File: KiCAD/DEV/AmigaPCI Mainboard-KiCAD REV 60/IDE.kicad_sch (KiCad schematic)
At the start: 55 parts, among them CN900 PRIMARY IDE, CN901 SECONDARY IDE, Q900 MMBT3906, U220 74LVC08, U815 74LVC08, U900 74LVC245, U901 74LVC245, U902 74LVC245, U903 74LVC245, U904 74LVC245, U905 74LVC245, U906 74LVC373, U907 74LVC373

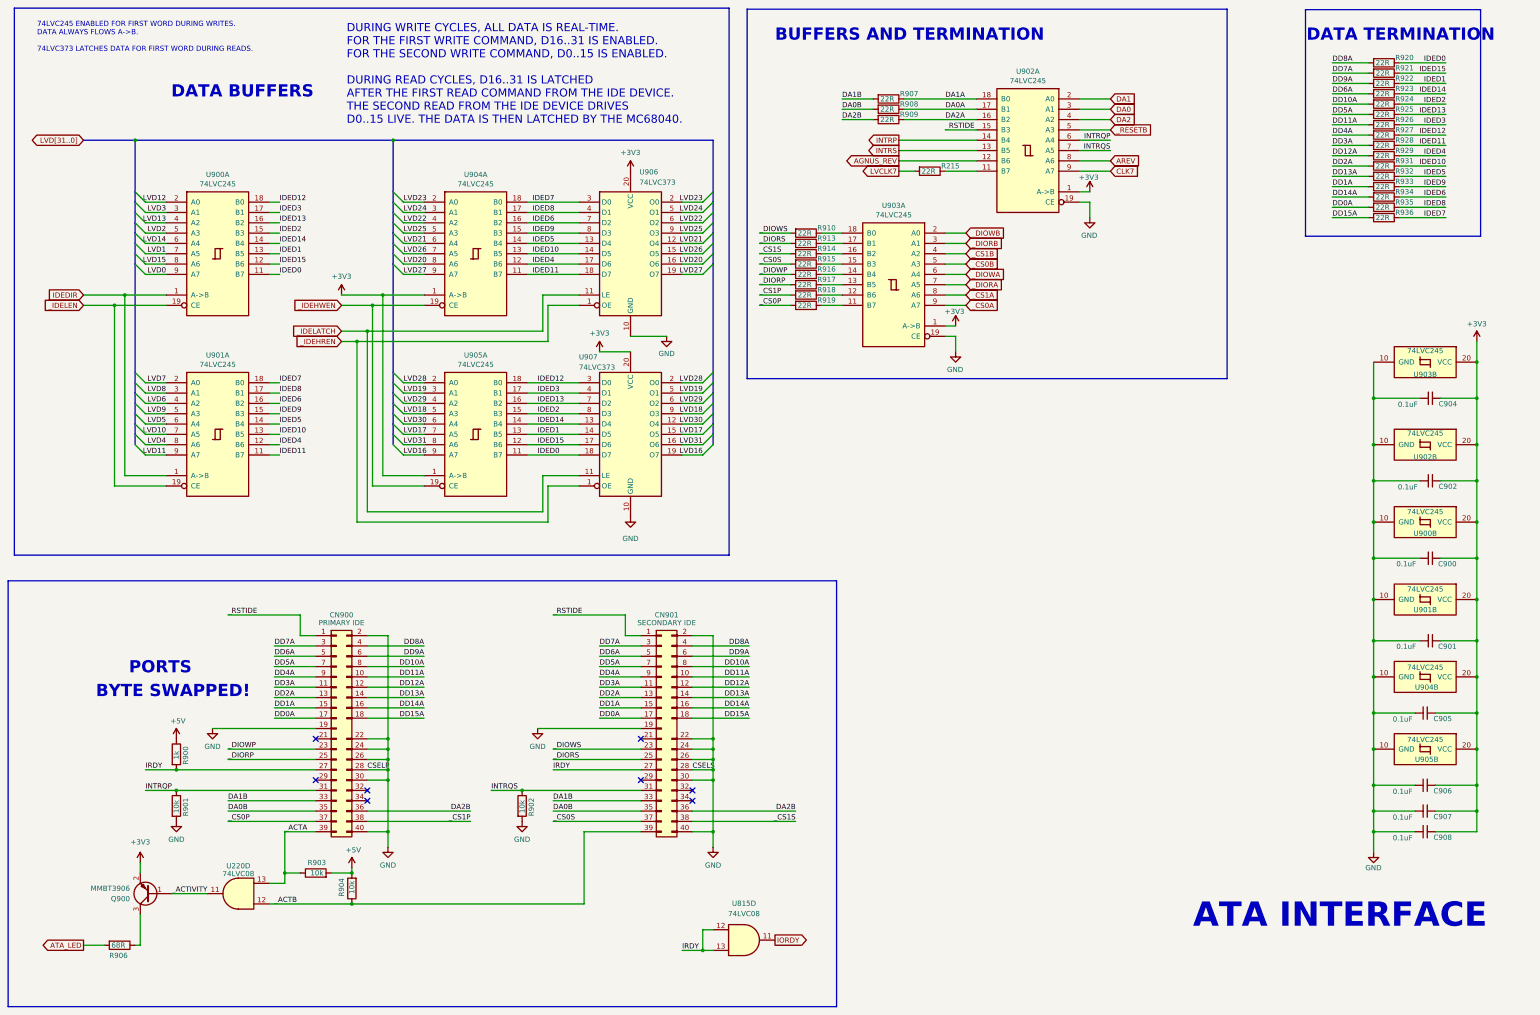
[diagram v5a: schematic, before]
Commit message: APCI Rev 6.0 Work
Added flash and i2c, USB now powered by standbay rail.
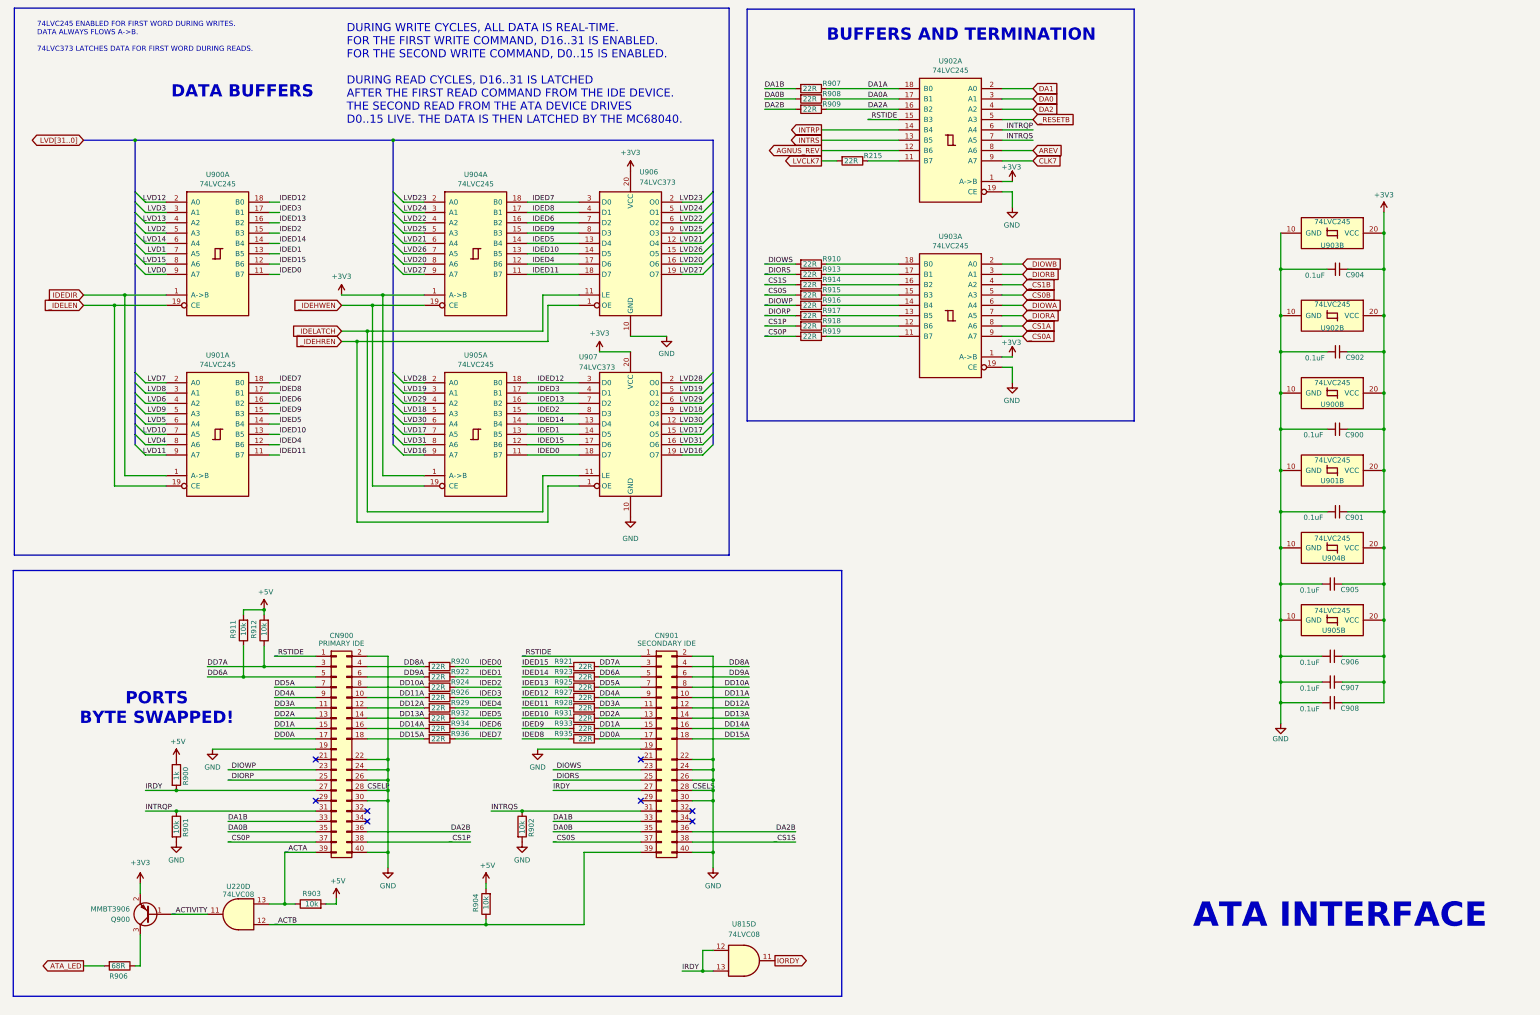
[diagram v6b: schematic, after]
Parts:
- added R911, R912: 10k, Resistor_SMD:R_0603_1608Metric, symbol Device:R
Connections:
- net +5V: now also R911.2, R912.2
- net DD6A: now also R911.1
- net DD7A: now also R912.1
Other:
- note added: "DURING WRITE CYCLES, ALL DATA IS REAL-TIME. FOR THE FIRST WRITE COMMAND, D16..31 IS ENABLED. FOR THE SECOND WRITE COMMAND, D0..15 IS ENABLED. DURING READ CYCLES, D16..31 IS LATCHED AFTER THE FIRST READ COMMAND FROM THE IDE DEVICE. THE SECOND READ FROM THE ATA DEVICE DRIVES D0..15 LIVE. THE DATA IS THEN LATCHED BY THE MC68040."
- note added: "PORTS BYTE SWAPPED!"
- note removed: "BYTE SWAPPED!"
- note removed: "DATA TERMINATION"
- note removed: "DURING WRITE CYCLES, ALL DATA IS REAL-TIME. FOR THE FIRST WRITE COMMAND, D16..31 IS ENABLED. FOR THE SECOND WRITE COMMAND, D0..15 IS ENABLED. DURING READ CYCLES, D16..31 IS LATCHED AFTER THE FIRST READ COMMAND FROM THE IDE DEVICE. THE SECOND READ FROM THE IDE DEVICE DRIVES D0..15 LIVE. THE DATA IS THEN LATCHED BY THE MC68040."
- note removed: "PORTS"
- moved on the sheet: C900, C901, C902, C904, C905, C906, C907, C908, CN900, CN901, Q900, R215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

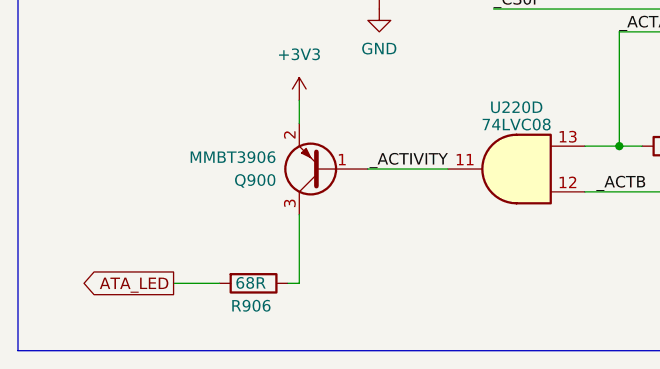
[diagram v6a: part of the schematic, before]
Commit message: APCI Added _LBEN pullup.
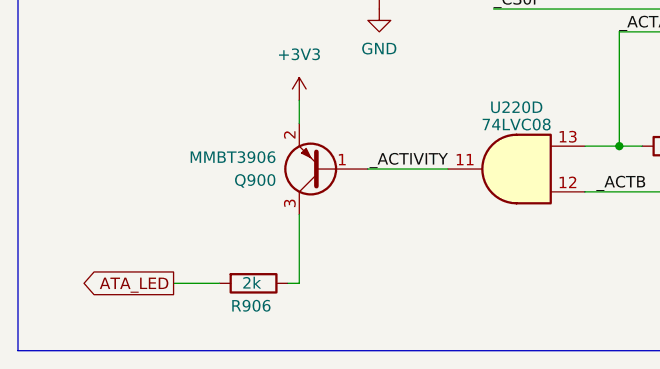
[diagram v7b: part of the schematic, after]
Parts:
- R906: value 68R -> 2k
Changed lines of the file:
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@@
 			)
 		)
-		(property "Value" "68R"
-			(at 46.228 255.27 90)
+		(property "Value" "2k"
+			(at 46.99 255.27 90)
 			(effects
 				(font
